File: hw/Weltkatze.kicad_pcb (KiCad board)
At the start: 4 copper layers, 109.3 x 58.9 mm, 106 parts, among them J1 USB_C_Receptacle_USB2.0_14P, J2 CONN_BAT, J3 PWR, J4 LED_OUT, J6 UART, J7 ESP_PWR, SW1 SW_SPDT, SW2 SW_Push, SW3 SW_Push, U1 TPS3700DDCR, U2 TP4056, U3 TPS61023DRLR, U5 TPS2111APW, U6 SPX3819M5-L-3-3, U7 BMP280, U8 LSM303C, U9 ESP32-C6-MINI-1/U, Y1 32.768k

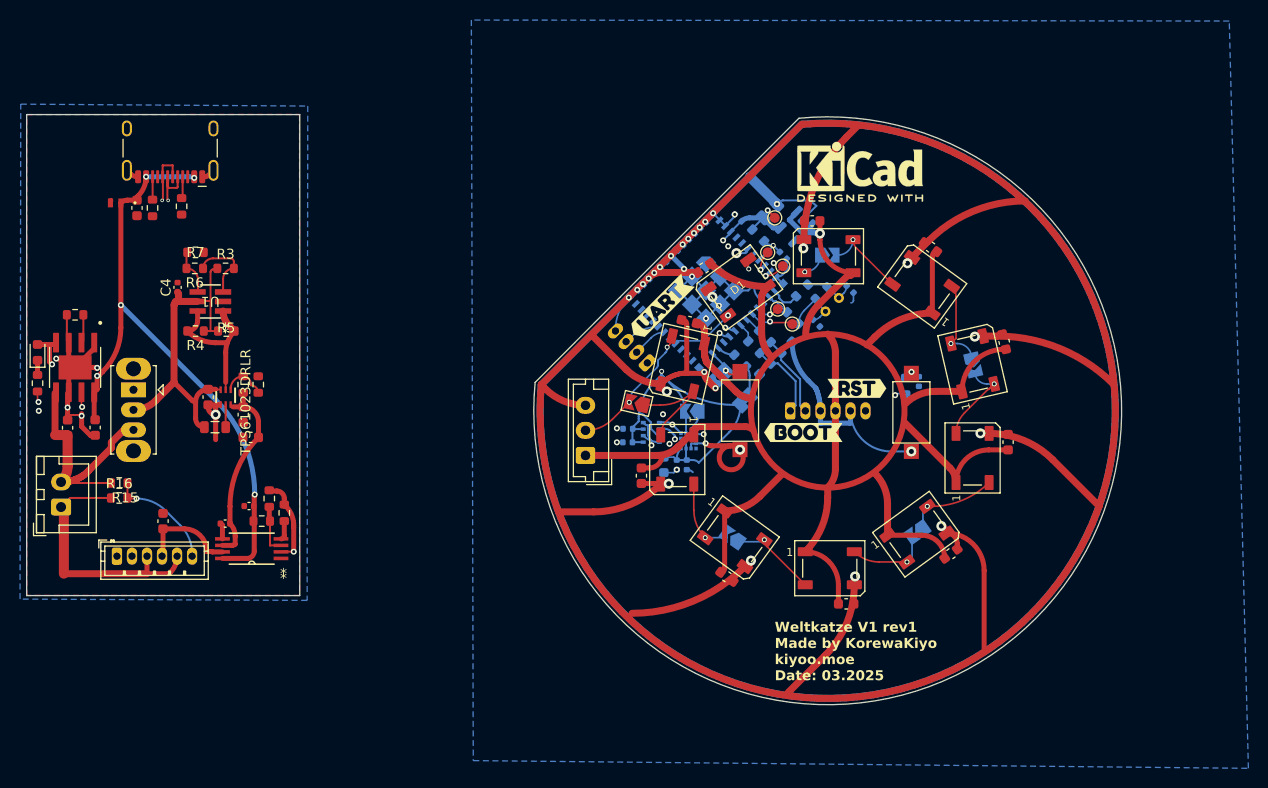
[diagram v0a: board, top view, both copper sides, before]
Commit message: V1 REV1 Final!
I consider this design finished, as such I've submitted it to JLCPCB

I converted to a 6L pcb because its cheaper, in.3 and in.4 have no copper
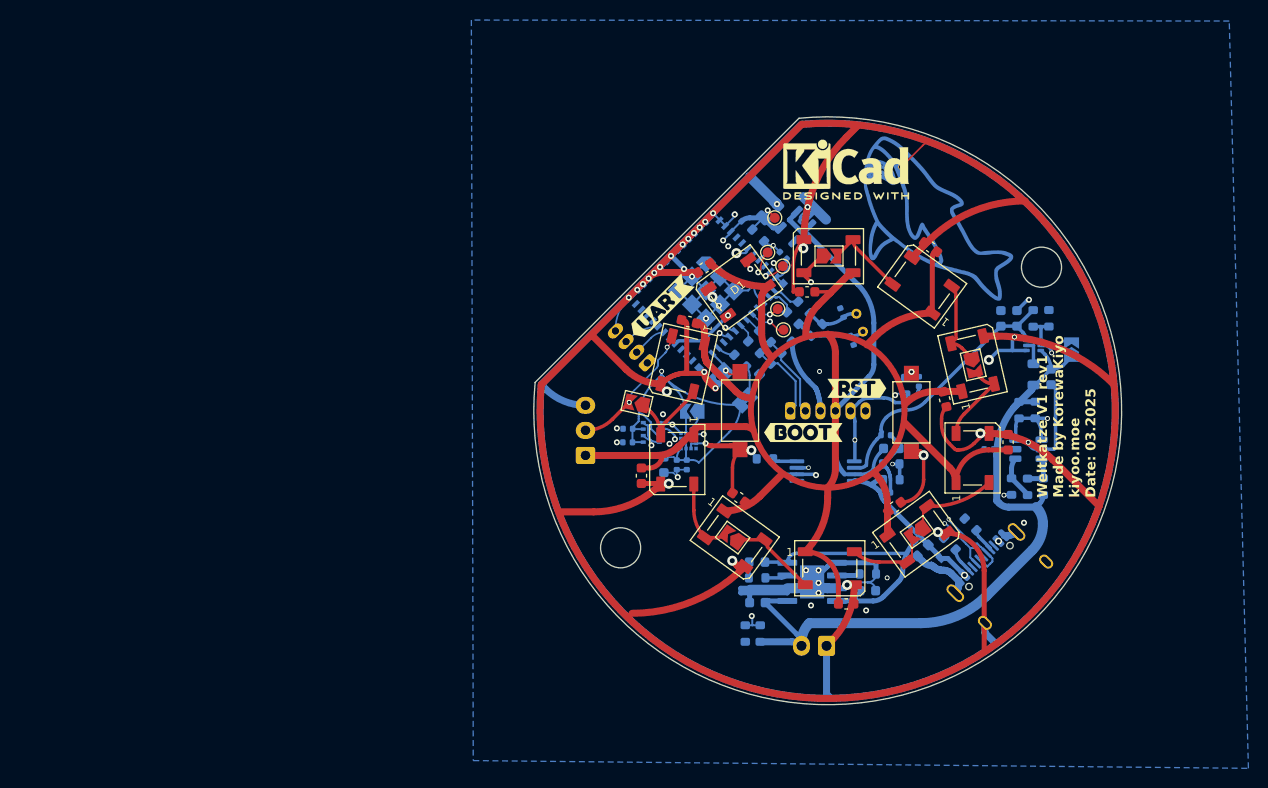
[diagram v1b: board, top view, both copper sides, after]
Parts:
- removed J3: PWR, Connector_JST:JST_ZH_B6B-ZR_1x06_P1.50mm_Vertical
- removed SW1: SW_SPDT, Button_Switch_THT:SW_Slide_SPDT_Straight_CK_OS102011MS2Q
- added G***: LOGO, Kiyo:Blahaj Exposed copper, B.Cu at (151.2, 67.5)
- added REF**: SolderJumper-2_P1.3mm_Open_TrianglePad1.0x1.5mm, Jumper:SolderJumper-2_P1.3mm_Open_TrianglePad1.0x1.5mm, B.Cu at (169.0, 85.7)
- added kibuzzard-67CB1547: G***, kibuzzard-67CB1547, B.Cu at (151.0, 115.6)
- added kibuzzard-67CB17AB: G***, kibuzzard-67CB17AB, B.Cu at (120.6, 103.1)
- C1, C10, C2, C3, C5, C6, C7, CR1, D1, J1, J2, J4, L1, R1, R10, R11, R12, R13, R14, R15, R16, R2, R4, R5, R6, R7, R8, R9, U2: moved to B.Cu
- C25, C26, C28, C29, C30: value 0.1u -> 100n
- C4, C8, C9: value 0.1u -> 100n; moved to B.Cu
- JP1, JP2, JP3, JP4: moved to F.Cu
- R3: value 597k -> 604k; moved to B.Cu
- U1: footprint lib:DDC6_TEX-M -> PCM_Package_TO_SOT_SMD_AKL:TSOT-23-6; moved to B.Cu
- U3: footprint lib:DRL0006A -> Package_TO_SOT_SMD:SOT-563; moved to B.Cu
- U5: footprint lib:PW8 -> Package_SO:TSSOP-8_4.4x3mm_P0.65mm; moved to B.Cu
- moved J1 94.7 mm to (162.7, 109.2), turned to -135 degrees
- moved CR1 89.4 mm to (155.5, 106.9), turned to -135 degrees
- moved R2 86.3 mm to (156.8, 105.1), turned to 135 degrees
- moved R6 85.9 mm to (164.6, 99.4), turned to -90 degrees
- moved C1 85.5 mm to (154.2, 105.8), turned to -135 degrees
- moved R1 84.9 mm to (158.9, 103.2), turned to 135 degrees
- moved R7 84.7 mm to (163.0, 99.4), turned to -90 degrees
- moved R3 84.5 mm to (166.2, 99.4), turned to 90 degrees
- moved C5 84.1 mm to (166.9, 88.5)
- moved R9 83.2 mm to (148.7, 108.1), turned to 0 degrees
- moved U1 83.0 mm to (164.7, 95.7)
- moved C4 82.6 mm to (160.8, 95.7), turned to 180 degrees
- moved R4 82.6 mm to (163.8, 91.8), turned to -90 degrees
- moved L1 81.8 mm to (165.2, 88.2), turned to 90 degrees
- moved R5 81.1 mm to (165.4, 91.8), turned to -90 degrees
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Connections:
- C4 pad 1: /Power/VBAT_SW -> VBAT
- C5 pad 1: /Power/VBAT_SW -> VBAT
- J1 pad A6: /Power/USBD_P -> /Logic/USBD_P
- J1 pad A7: /Power/USBD_N -> /Logic/USBD_N
- J1 pad A8: (no net) -> unconnected-(J1-SBU1-PadA8)
- J1 pad B6: /Power/USBD_P -> /Logic/USBD_P
- J1 pad B7: /Power/USBD_N -> /Logic/USBD_N
- J1 pad B8: (no net) -> unconnected-(J1-SBU2-PadB8)
- L1 pad 1: /Power/VBAT_SW -> VBAT
- R3 pad 1: /Power/VBAT_SW -> VBAT
- R4 pad 1: /Power/VBAT_SW -> VBAT
- R5 pad 1: /Power/VBAT_SW -> VBAT
- U1 pad 5: /Power/VBAT_SW -> VBAT
- U3 pad 3: /Power/VBAT_SW -> VBAT
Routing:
- net VBAT: track 24.2 -> 74.2 mm
- net /Power/USBD_P: track 43.1 -> 0.00 mm, vias 1 -> 0
- net /Power/USBD_N: track 43.0 -> 0.00 mm, vias 1 -> 0
- net GND: track 388.9 -> 428.2 mm, vias 55 -> 57
- net /Power/VBAT_SW: track 34.2 -> 0.00 mm
- net /Logic/USBD_N: track 8.25 -> 41.7 mm, vias 0 -> 1
- net /Logic/USBD_P: track 7.89 -> 40.6 mm, vias 0 -> 1
- net /Power/USB_VBUS: track 73.4 -> 49.0 mm, vias 6 -> 2
- net /Logic/VBAT_MON: track 32.9 -> 53.1 mm
- net /Power/VBUS: track 19.4 -> 27.2 mm
- net Net-(U5-VSNS): track 4.87 -> 11.9 mm, vias 0 -> 2
- net Net-(U2-~{CHRG}): track 7.05 -> 2.24 mm, vias 2 -> 0
- net +5V: track 173.4 -> 169.3 mm, vias 1 -> 0
- net Net-(U1-INA+): track 7.37 -> 3.56 mm
- net /Power/VBAT_EN: track 15.3 -> 17.9 mm, vias 0 -> 2
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- removed copper zone on F.Cu, net GND
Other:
- board size 109.3 x 58.9 mm -> 58.7 x 58.7 mm
- copper layers 4 -> 6

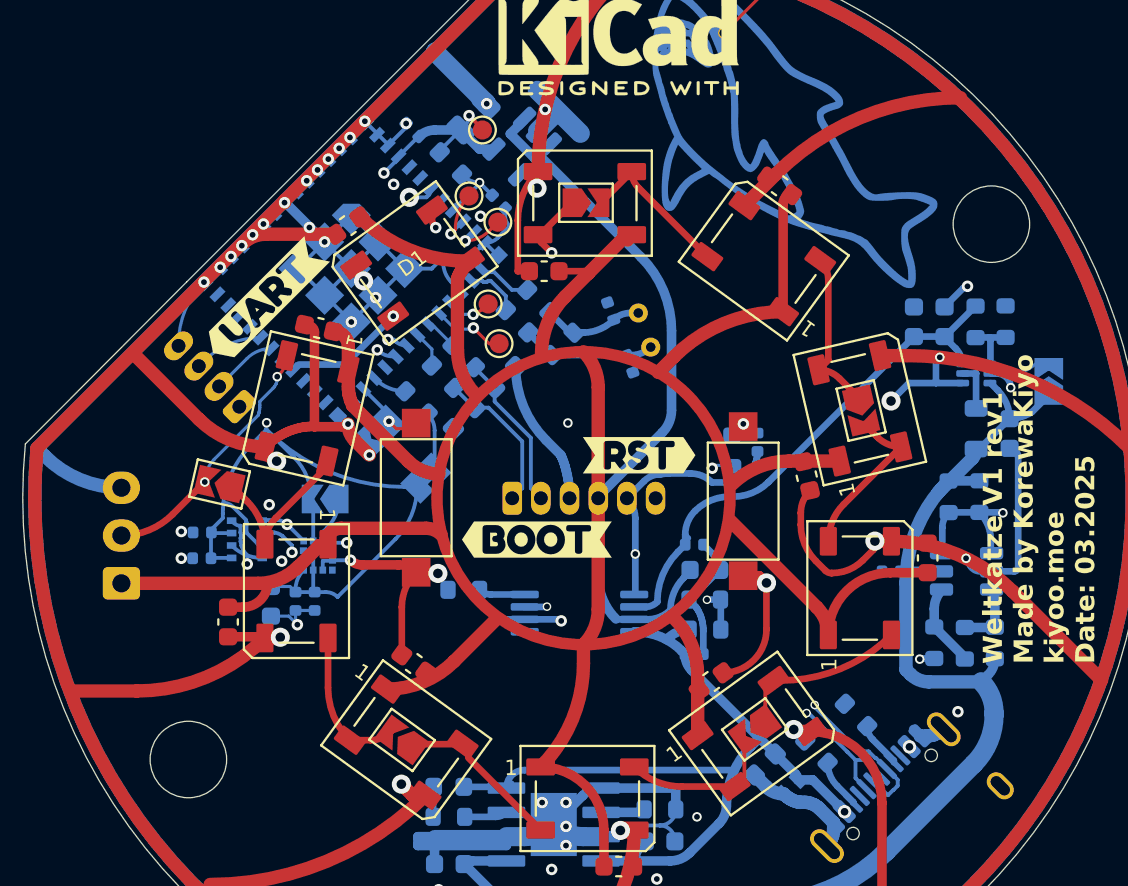
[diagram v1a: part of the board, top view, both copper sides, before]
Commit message: rev1.5
Update to use 6 layers, inc one for 5V

Can possibly eliminate all front copper but i like how it looks
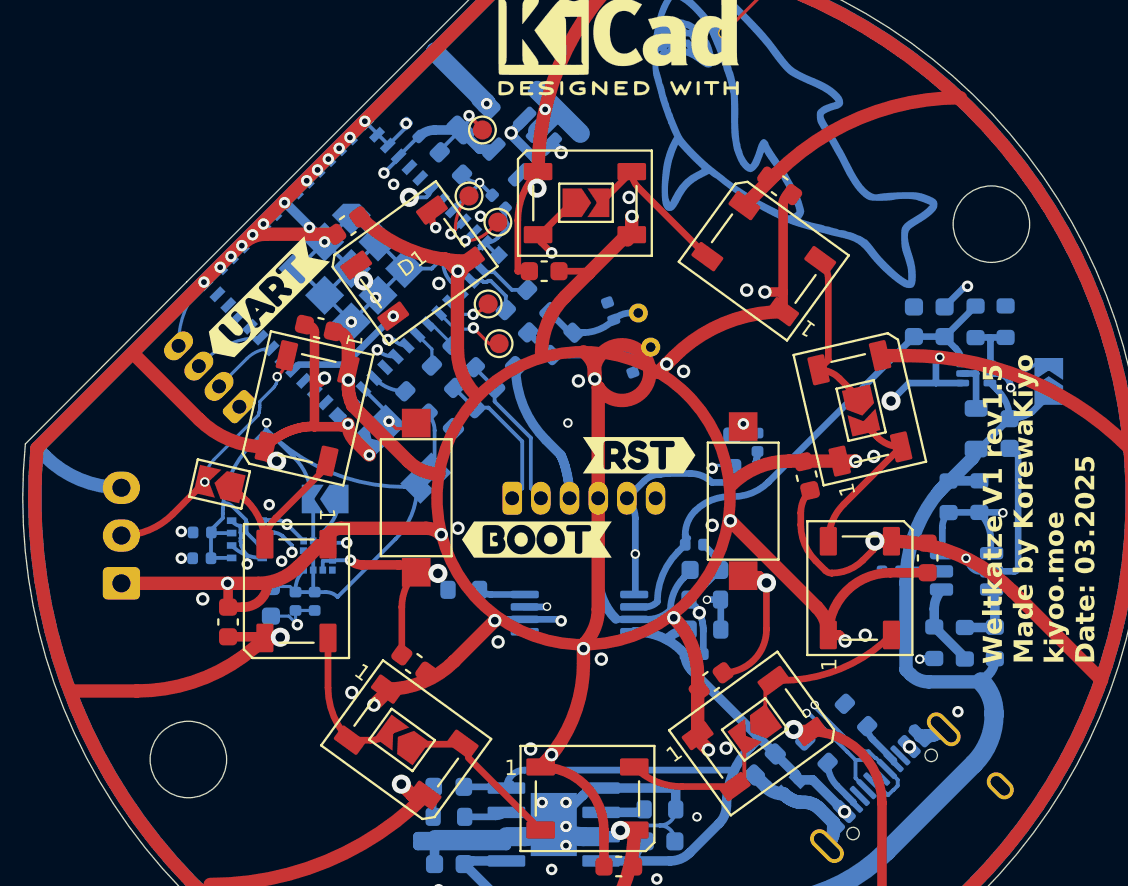
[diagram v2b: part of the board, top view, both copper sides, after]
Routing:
- net +5V: track 169.3 -> 158.8 mm, vias 0 -> 19
- net GND: track 428.2 -> 428.8 mm, vias 57 -> 74
- added copper zone on In2.Cu, net +5V
- added copper zone on In3.Cu, net GND
- added copper zone on In4.Cu, net GND
- removed copper zone on In2.Cu, net GND
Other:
- board text added: "Weltkatze V1 rev1.5 Made by KorewaKiyo kiyoo.moe Date: 03.2025"
- board text removed: "Weltkatze V1 rev1 Made by KorewaKiyo kiyoo.moe Date: 03.2025"

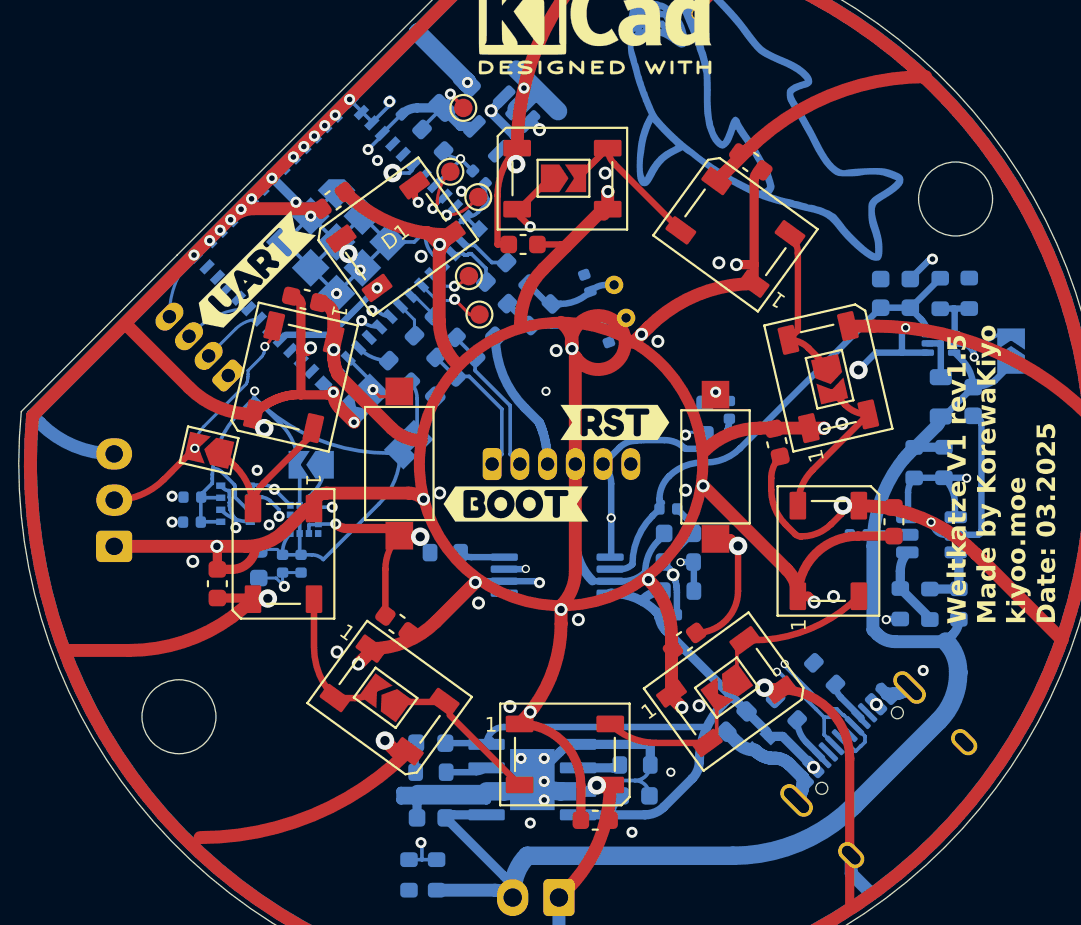
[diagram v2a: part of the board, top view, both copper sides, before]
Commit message: Minor reroute
Minor reroute of traces, utilises all 6 layers effectively now.
Also reduces some issues with USB going through multiple layers unnecessarily
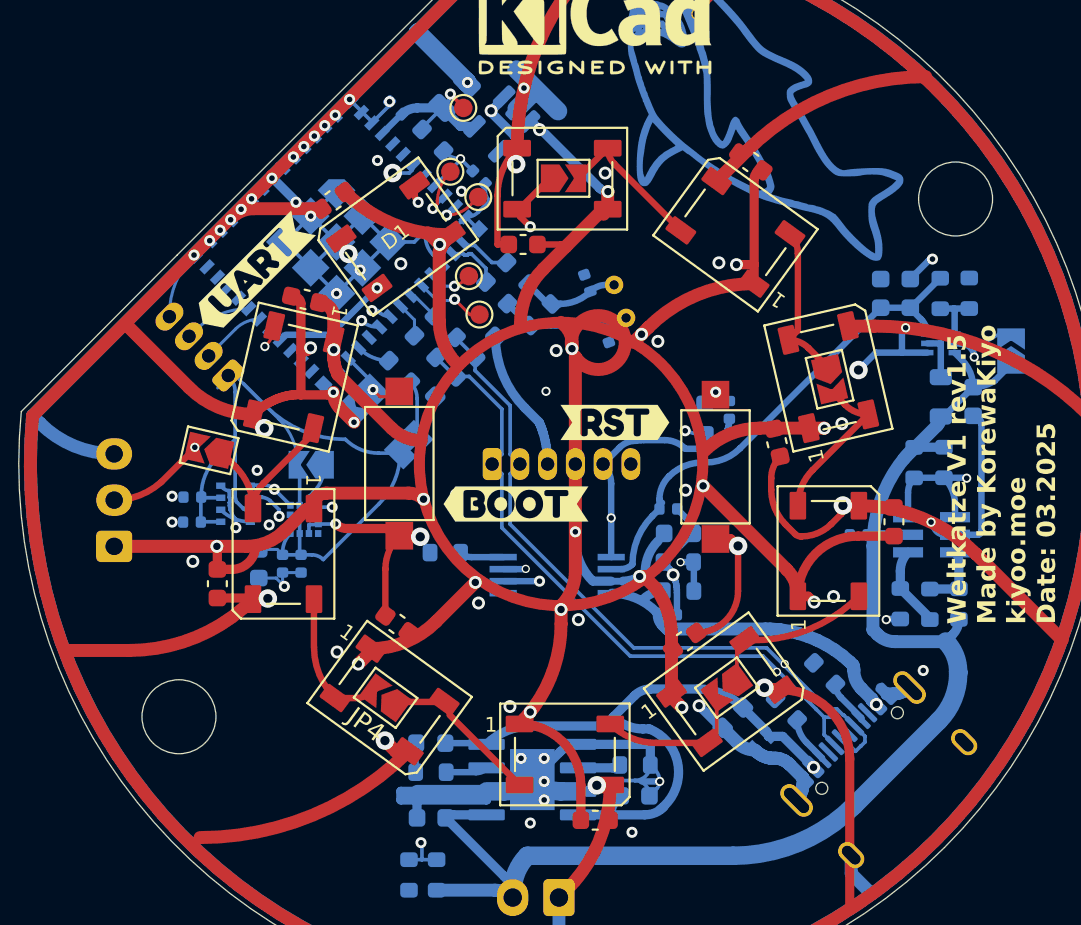
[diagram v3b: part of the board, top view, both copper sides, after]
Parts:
- C25, C26, C28, C29, C30, C4, C8, C9: value 100n -> 0.1u
- R3: value 604k -> 597k
- U1: footprint PCM_Package_TO_SOT_SMD_AKL:TSOT-23-6 -> lib:DDC6_TEX-M
- U3: footprint Package_TO_SOT_SMD:SOT-563 -> lib:DRL0006A
- U5: footprint Package_SO:TSSOP-8_4.4x3mm_P0.65mm -> lib:PW8
- moved C1 0.29 mm to (154.0, 105.5)
- moved CR1 0.06 mm to (155.5, 106.9)
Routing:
- net +3V3: track 70.9 -> 80.2 mm, vias 3 -> 1
- net +5V: track 158.8 -> 164.2 mm, vias 19 -> 22
- net /Power/USB_VBUS: track 49.0 -> 53.3 mm
- net /Logic/USBD_P: track 40.6 -> 36.9 mm
- net /Logic/USBD_N: track 41.7 -> 38.1 mm
- net GND: track 428.8 -> 426.0 mm
- net Net-(D11-DOUT): track 13.5 -> 14.7 mm

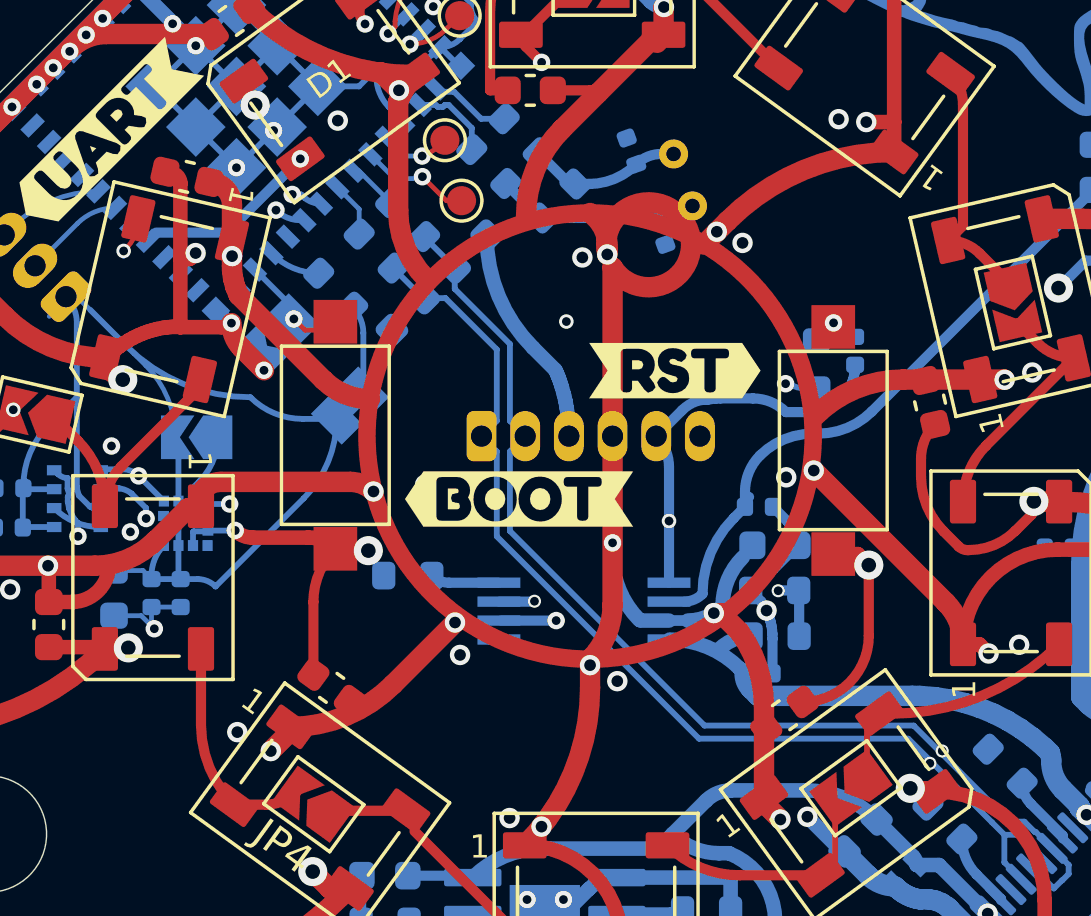
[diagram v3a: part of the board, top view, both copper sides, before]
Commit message: Update to kicad v9
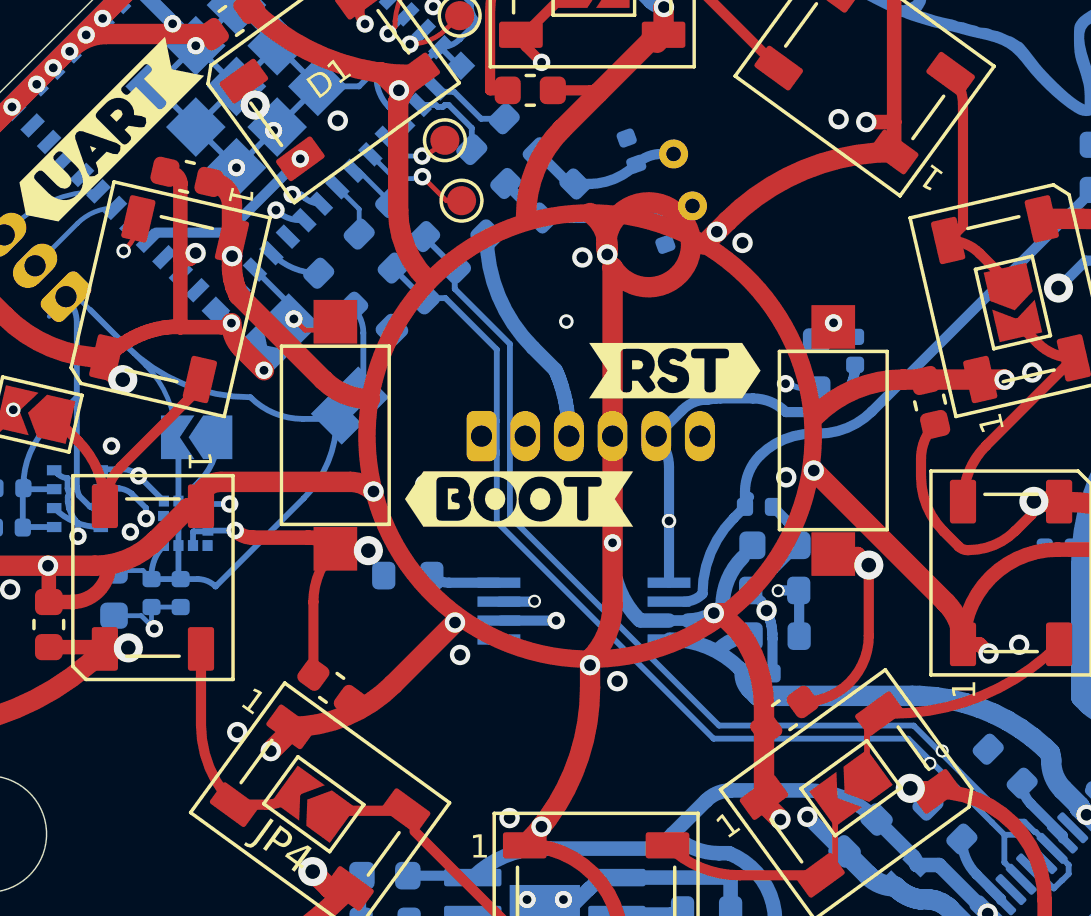
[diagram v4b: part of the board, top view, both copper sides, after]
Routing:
- net /Logic/USBD_P: track 36.9 -> 37.7 mm
- net /Logic/USBD_N: track 38.1 -> 37.4 mm
